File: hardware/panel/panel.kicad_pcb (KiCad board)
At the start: 2 copper layers, 62 x 104.3 mm, 1 part

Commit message: Panel: real MT1-MT4 standoff footprints (BOM/pos visible); combined file now flush V-cut seam
Standoff seats become SMD footprints with mask+paste aperture pads over the
back flood, so PCBWay's assembly sees 4 reflow nuts on the bottom side.
combine_boards.py butts the boards flush with one straight V-score at y=60 —
a sandable seam instead of mouse-bite nubs. Part number for the nut pends
sourcing (STANDOFF_PART/STANDOFF_LCSC in emit_board.py).
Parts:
- added MT1: SMTSO-M2.5-3ET, panel:SMT_Standoff_M2.5_D5.0mm, B.Cu at (5.64, 5.64)
- added MT2: SMTSO-M2.5-3ET, panel:SMT_Standoff_M2.5_D5.0mm, B.Cu at (56.4, 5.64)
- added MT3: SMTSO-M2.5-3ET, panel:SMT_Standoff_M2.5_D5.0mm, B.Cu at (5.64, 91.9)
- added MT4: SMTSO-M2.5-3ET, panel:SMT_Standoff_M2.5_D5.0mm, B.Cu at (53.4, 91.9)

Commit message: Panel: Wurth 9774030151R flat-bottom M2.5x3 standoffs — 6.0mm seats, ring paste, assembly data
Sourcing: no boss-free M2.5x3 exists except this Wurth WA-SMSI spacer
(Digi-Key, 48k stock). Seat grown 5.0->6.0mm per its land pattern; paste is
a 5.8/3.9mm ring so solder can't wick into the bottom-resident thread. Case
plan flag: screw tip must stop ~0.5mm short of the seat. MT1-4 now appear
in panel-bom/pos and the combined assembly BOM.
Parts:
- MT1: renamed from MT3; value SMTSO-M2.5-3ET -> 9774030151R; footprint panel:SMT_Standoff_M2.5_D5.0mm -> panel:SMT_Standoff_M2.5_D6.0mm
- MT2, MT4: value SMTSO-M2.5-3ET -> 9774030151R; footprint panel:SMT_Standoff_M2.5_D5.0mm -> panel:SMT_Standoff_M2.5_D6.0mm
- MT3: renamed from MT1; value SMTSO-M2.5-3ET -> 9774030151R; footprint panel:SMT_Standoff_M2.5_D5.0mm -> panel:SMT_Standoff_M2.5_D6.0mm
- moved MT1 86.3 mm to (5.64, 5.64)
- moved MT3 86.3 mm to (5.64, 91.9)

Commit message: Combined panel: flip art board face-down for one-sided assembly; nut 3D model
Panel mirrors left-right about its centreline inside the production panel,
so the standoff nuts reflow on the same face as the main board's SMT — a
single-side assembly order. Physical boards unchanged. Standoffs get a
5.1x3mm cylinder wrl so they show in 3D/renders.
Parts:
- moved MT2 86.3 mm to (56.4, 5.64)
- moved MT3 86.3 mm to (5.64, 91.9)
- moved MT1 50.7 mm to (5.64, 5.64)
- moved MT4 47.7 mm to (53.4, 91.9)
- renumbered MT2 to MT1, MT4 to MT2, MT1 to MT3, MT3 to MT4
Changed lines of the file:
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@@
+	(footprint "panel:SMT_Standoff_M2.5_D6.0mm"
+		(layer "B.Cu")
+		(at 5.6364 91.93)
+		(property "Reference" "MT3"
+			(at 0 0 0)
+			(layer "F.SilkS")
+			(hide yes)
+			(effects
+				(font
+					(size 1.27 1.27)
+				)
+			)
+		)
+		(property "Value" "9774030151R"
+			(at 0 0 0)
+			(layer "F.Fab")
+			(hide yes)
+			(effects
+				(font
+					(size 1.27 1.27)
+				)
+			)
+		)
+		(property "Datasheet" ""
+			(at 0 0 0)
+			(layer "F.Fab")
+			(hide yes)
+			(effects
+				(font
+					(size 1.27 1.27)
+				)
+			)
+		)
+		(property "Description" ""
+			(at 0 0 0)
+			(layer "F.Fab")
+			(hide yes)
+			(effects
+				(font
+					(size 1.27 1.27)
+				)
+			)
+		)
+		(attr smd)
+		(duplicate_pad_numbers_are_jumpers no)
+		(pad "" smd circle
+			(at 0 0)
+			(size 6 6)
+			(layers "B.Mask")
+		)
+		(embedded_fonts no)
+		(model "${KIPRJMOD}/standoff-m25x3.wrl"
+			(offset
+				(xyz 0 0 0)
+			)
+			(scale
+				(xyz 1 1 1)
+			)
+			(rotate
+				(xyz 0 0 0)
+			)
+		)
+	)
+	(footprint "panel:SMT_Standoff_M2.5_D6.0mm"
+		(layer "B.Cu")
+		(at 56.3636 5.6364)
+		(property "Reference" "MT2"
+			(at 0 0 0)
+			(layer "F.SilkS")
+			(hide yes)
+			(effects
+				(font
+					(size 1.27 1.27)
+				)
+			)
+		)
+		(property "Value" "9774030151R"
+			(at 0 0 0)
+			(layer "F.Fab")
+			(hide yes)
+			(effects
+				(font
+					(size 1.27 1.27)
+				)
+			)
+		)
+		(property "Datasheet" ""
+			(at 0 0 0)
+			(layer "F.Fab")
+			(hide yes)
+			(effects
+				(font
+					(size 1.27 1.27)
+				)
+			)
+		)
+		(property "Description" ""
+			(at 0 0 0)
+			(layer "F.Fab")
+			(hide yes)
+			(effects
+				(font
+					(size 1.27 1.27)
+				)
+			)
+		)
+		(attr smd)
+		(duplicate_pad_numbers_are_jumpers no)
+		(pad "" smd circle
+			(at 0 0)
+			(size 6 6)
+			(layers "B.Mask")
+		)
+		(embedded_fonts no)
+		(model "${KIPRJMOD}/standoff-m25x3.wrl"
+			(offset
+				(xyz 0 0 0)
+			)
+			(scale
+				(xyz 1 1 1)
+			)
+			(rotate
+				(xyz 0 0 0)
+			)
+		)
+	)
+	(footprint "panel:SMT_Standoff_M2.5_D6.0mm"
+		(layer "B.Cu")
+		(at 53.3636 91.93)
+		(property "Reference" "MT4"
+			(at 0 0 0)
+			(layer "F.SilkS")
+			(hide yes)
+			(effects
+				(font
+					(size 1.27 1.27)
+				)
+			)
+		)
+		(property "Value" "9774030151R"
+			(at 0 0 0)
+			(layer "F.Fab")
+			(hide yes)
+			(effects
+				(font
+					(size 1.27 1.27)
+				)
+			)
+		)
+		(property "Datasheet" ""
+			(at 0 0 0)
+			(layer "F.Fab")
+			(hide yes)
+			(effects
+				(font
+					(size 1.27 1.27)
+				)
+			)
+		)
+		(property "Description" ""
+			(at 0 0 0)
+			(layer "F.Fab")
+			(hide yes)
+			(effects
+				(font
+					(size 1.27 1.27)
+				)
+			)
+		)
+		(attr smd)
+		(duplicate_pad_numbers_are_jumpers no)
+		(pad "" smd circle
+			(at 0 0)
+			(size 6 6)
+			(layers "B.Mask")
+		)
+		(embedded_fonts no)
+		(model "${KIPRJMOD}/standoff-m25x3.wrl"
+			(offset
+				(xyz 0 0 0)
+			)
+			(scale
+				(xyz 1 1 1)
+			)
+			(rotate
+				(xyz 0 0 0)
+			)
+		)
+	)
 	(footprint "panel:SMT_Standoff_M2.5_D6.0mm"
 		(layer "B.Cu")
@@
 		)
 		(embedded_fonts no)
-	)
-	(footprint "panel:SMT_Standoff_M2.5_D6.0mm"
-		(layer "B.Cu")
-		(at 53.3636 91.93)
-		(property "Reference" "MT4"
-			(at 0 0 0)
-			(layer "F.SilkS")
-			(hide yes)
-			(effects
-				(font
-					(size 1.27 1.27)
-				)
-			)
-		)
-		(property "Value" "9774030151R"
-			(at 0 0 0)
-			(layer "F.Fab")
-			(hide yes)
-			(effects
-				(font
-					(size 1.27 1.27)
-				)
-			)
-		)
-		(property "Datasheet" ""
-			(at 0 0 0)
-			(layer "F.Fab")
-			(hide yes)
-			(effects
-				(font
-					(size 1.27 1.27)
-				)
-			)
-		)
-		(property "Description" ""
-			(at 0 0 0)
-			(layer "F.Fab")
-			(hide yes)
-			(effects
-				(font
-					(size 1.27 1.27)
-				)
-			)
-		)
-		(attr smd)
-		(duplicate_pad_numbers_are_jumpers no)
-		(pad "" smd circle
-			(at 0 0)
-			(size 6 6)
-			(layers "B.Mask")
-		)
-		(embedded_fonts no)
-	)
-	(footprint "panel:SMT_Standoff_M2.5_D6.0mm"
-		(layer "B.Cu")
-		(at 5.6364 91.93)
-		(property "Reference" "MT3"
-			(at 0 0 0)
-			(layer "F.SilkS")
-			(hide yes)
-			(effects
-				(font
-					(size 1.27 1.27)
-				)
-			)
-		)
-		(property "Value" "9774030151R"
-			(at 0 0 0)
-			(layer "F.Fab")
-			(hide yes)
-			(effects
-				(font
-					(size 1.27 1.27)
-				)
-			)
-		)
-		(property "Datasheet" ""
-			(at 0 0 0)
-			(layer "F.Fab")
-			(hide yes)
-			(effects
-				(font
-					(size 1.27 1.27)
-				)
-			)
-		)
-		(property "Description" ""
-			(at 0 0 0)
-			(layer "F.Fab")
-			(hide yes)
-			(effects
-				(font
-					(size 1.27 1.27)
-				)
-			)
-		)
-		(attr smd)
-		(duplicate_pad_numbers_are_jumpers no)
-		(pad "" smd circle
-			(at 0 0)
-			(size 6 6)
-			(layers "B.Mask")
-		)
-		(embedded_fonts no)
-	)
-	(footprint "panel:SMT_Standoff_M2.5_D6.0mm"
-		(layer "B.Cu")
-		(at 56.3636 5.6364)
-		(property "Reference" "MT2"
-			(at 0 0 0)
-			(layer "F.SilkS")
-			(hide yes)
-			(effects
-				(font
-					(size 1.27 1.27)
-				)
-			)
-		)
-		(property "Value" "9774030151R"
-			(at 0 0 0)
-			(layer "F.Fab")
-			(hide yes)
-			(effects
-				(font
-					(size 1.27 1.27)
-				)
-			)
-		)
-		(property "Datasheet" ""
-			(at 0 0 0)
-			(layer "F.Fab")
-			(hide yes)
-			(effects
-				(font
-					(size 1.27 1.27)
-				)
-			)
-		)
-		(property "Description" ""
-			(at 0 0 0)
-			(layer "F.Fab")
-			(hide yes)
-			(effects
-				(font
-					(size 1.27 1.27)
-				)
-			)
-		)
-		(attr smd)
-		(duplicate_pad_numbers_are_jumpers no)
-		(pad "" smd circle
-			(at 0 0)
-			(size 6 6)
-			(layers "B.Mask")
-		)
-		(embedded_fonts no)
+		(model "${KIPRJMOD}/standoff-m25x3.wrl"
+			(offset
+				(xyz 0 0 0)
+			)
+			(scale
+				(xyz 1 1 1)
+			)
+			(rotate
+				(xyz 0 0 0)
+			)
+		)
 	)
 	(gr_poly

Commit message: Standoffs: use KiCad's stock Wurth WA-SMSI H3mm STEP model (hand-written wrl never parsed)
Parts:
- moved MT3 47.7 mm to (5.64, 91.9)
- moved MT4 47.7 mm to (53.4, 91.9)
- renumbered MT4 to MT3, MT3 to MT4
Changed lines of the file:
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@@
+	(footprint "panel:SMT_Standoff_M2.5_D6.0mm"
+		(layer "B.Cu")
+		(at 53.3636 91.93)
+		(property "Reference" "MT4"
+			(at 0 0 0)
+			(layer "F.SilkS")
+			(hide yes)
+			(effects
+				(font
+					(size 1.27 1.27)
+				)
+			)
+		)
+		(property "Value" "9774030151R"
+			(at 0 0 0)
+			(layer "F.Fab")
+			(hide yes)
+			(effects
+				(font
+					(size 1.27 1.27)
+				)
+			)
+		)
+		(property "Datasheet" ""
+			(at 0 0 0)
+			(layer "F.Fab")
+			(hide yes)
+			(effects
+				(font
+					(size 1.27 1.27)
+				)
+			)
+		)
+		(property "Description" ""
+			(at 0 0 0)
+			(layer "F.Fab")
+			(hide yes)
+			(effects
+				(font
+					(size 1.27 1.27)
+				)
+			)
+		)
+		(attr smd)
+		(duplicate_pad_numbers_are_jumpers no)
+		(pad "" smd circle
+			(at 0 0)
+			(size 6 6)
+			(layers "B.Mask")
+		)
+		(embedded_fonts no)
+		(model "${KICAD10_3DMODEL_DIR}/Mounting_Wuerth.3dshapes/Mounting_Wuerth_WA-SMSI-M2.5_H3mm_9774030151.step"
+			(offset
+				(xyz 0 0 0)
+			)
+			(scale
+				(xyz 1 1 1)
+			)
+			(rotate
+				(xyz 0 0 0)
+			)
+		)
+	)
+	(footprint "panel:SMT_Standoff_M2.5_D6.0mm"
+		(layer "B.Cu")
+		(at 56.3636 5.6364)
+		(property "Reference" "MT2"
+			(at 0 0 0)
+			(layer "F.SilkS")
+			(hide yes)
+			(effects
+				(font
+					(size 1.27 1.27)
+				)
+			)
+		)
+		(property "Value" "9774030151R"
+			(at 0 0 0)
+			(layer "F.Fab")
+			(hide yes)
+			(effects
+				(font
+					(size 1.27 1.27)
+				)
+			)
+		)
+		(property "Datasheet" ""
+			(at 0 0 0)
+			(layer "F.Fab")
+			(hide yes)
+			(effects
+				(font
+					(size 1.27 1.27)
+				)
+			)
+		)
+		(property "Description" ""
+			(at 0 0 0)
+			(layer "F.Fab")
+			(hide yes)
+			(effects
+				(font
+					(size 1.27 1.27)
+				)
+			)
+		)
+		(attr smd)
+		(duplicate_pad_numbers_are_jumpers no)
+		(pad "" smd circle
+			(at 0 0)
+			(size 6 6)
+			(layers "B.Mask")
+		)
+		(embedded_fonts no)
+		(model "${KICAD10_3DMODEL_DIR}/Mounting_Wuerth.3dshapes/Mounting_Wuerth_WA-SMSI-M2.5_H3mm_9774030151.step"
+			(offset
+				(xyz 0 0 0)
+			)
+			(scale
+				(xyz 1 1 1)
+			)
+			(rotate
+				(xyz 0 0 0)
+			)
+		)
+	)
 	(footprint "panel:SMT_Standoff_M2.5_D6.0mm"
 		(layer "B.Cu")
@@
 		)
 		(embedded_fonts no)
-		(model "${KIPRJMOD}/standoff-m25x3.wrl"
+		(model "${KICAD10_3DMODEL_DIR}/Mounting_Wuerth.3dshapes/Mounting_Wuerth_WA-SMSI-M2.5_H3mm_9774030151.step"
 			(offset
 				(xyz 0 0 0)
@@
 	(footprint "panel:SMT_Standoff_M2.5_D6.0mm"
 		(layer "B.Cu")
-		(at 56.3636 5.6364)
-		(property "Reference" "MT2"
-			(at 0 0 0)
-			(layer "F.SilkS")
-			(hide yes)
-			(effects
-				(font
-					(size 1.27 1.27)
-				)
-			)
-		)
-		(property "Value" "9774030151R"
-			(at 0 0 0)
-			(layer "F.Fab")
-			(hide yes)
-			(effects
-				(font
-					(size 1.27 1.27)
-				)
-			)
-		)
-		(property "Datasheet" ""
-			(at 0 0 0)
-			(layer "F.Fab")
-			(hide yes)
-			(effects
-				(font
-					(size 1.27 1.27)
-				)
-			)
-		)
-		(property "Description" ""
-			(at 0 0 0)
-			(layer "F.Fab")
-			(hide yes)
-			(effects
-				(font
-					(size 1.27 1.27)
-				)
-			)
-		)
-		(attr smd)
-		(duplicate_pad_numbers_are_jumpers no)
-		(pad "" smd circle
-			(at 0 0)
-			(size 6 6)
-			(layers "B.Mask")
-		)
-		(embedded_fonts no)
-		(model "${KIPRJMOD}/standoff-m25x3.wrl"
-			(offset
-				(xyz 0 0 0)
-			)
-			(scale
-				(xyz 1 1 1)
-			)
-			(rotate
-				(xyz 0 0 0)
-			)
-		)
-	)
-	(footprint "panel:SMT_Standoff_M2.5_D6.0mm"
-		(layer "B.Cu")
-		(at 53.3636 91.93)
-		(property "Reference" "MT4"
-			(at 0 0 0)
-			(layer "F.SilkS")
-			(hide yes)
-			(effects
-				(font
-					(size 1.27 1.27)
-				)
-			)
-		)
-		(property "Value" "9774030151R"
-			(at 0 0 0)
-			(layer "F.Fab")
-			(hide yes)
-			(effects
-				(font
-					(size 1.27 1.27)
-				)
-			)
-		)
-		(property "Datasheet" ""
-			(at 0 0 0)
-			(layer "F.Fab")
-			(hide yes)
-			(effects
-				(font
-					(size 1.27 1.27)
-				)
-			)
-		)
-		(property "Description" ""
-			(at 0 0 0)
-			(layer "F.Fab")
-			(hide yes)
-			(effects
-				(font
-					(size 1.27 1.27)
-				)
-			)
-		)
-		(attr smd)
-		(duplicate_pad_numbers_are_jumpers no)
-		(pad "" smd circle
-			(at 0 0)
-			(size 6 6)
-			(layers "B.Mask")
-		)
-		(embedded_fonts no)
-		(model "${KIPRJMOD}/standoff-m25x3.wrl"
-			(offset
-				(xyz 0 0 0)
-			)
-			(scale
-				(xyz 1 1 1)
-			)
-			(rotate
-				(xyz 0 0 0)
-			)
-		)
-	)
-	(footprint "panel:SMT_Standoff_M2.5_D6.0mm"
-		(layer "B.Cu")
 		(at 5.6364 5.6364)
 		(property "Reference" "MT1"
@@
 		)
 		(embedded_fonts no)
-		(model "${KIPRJMOD}/standoff-m25x3.wrl"
-			(offset
-				(xyz 0 0 0)
+		(model "${KICAD10_3DMODEL_DIR}/Mounting_Wuerth.3dshapes/Mounting_Wuerth_WA-SMSI-M2.5_H3mm_9774030151.step"
+			(offset
+				(xyz 0 0 0)

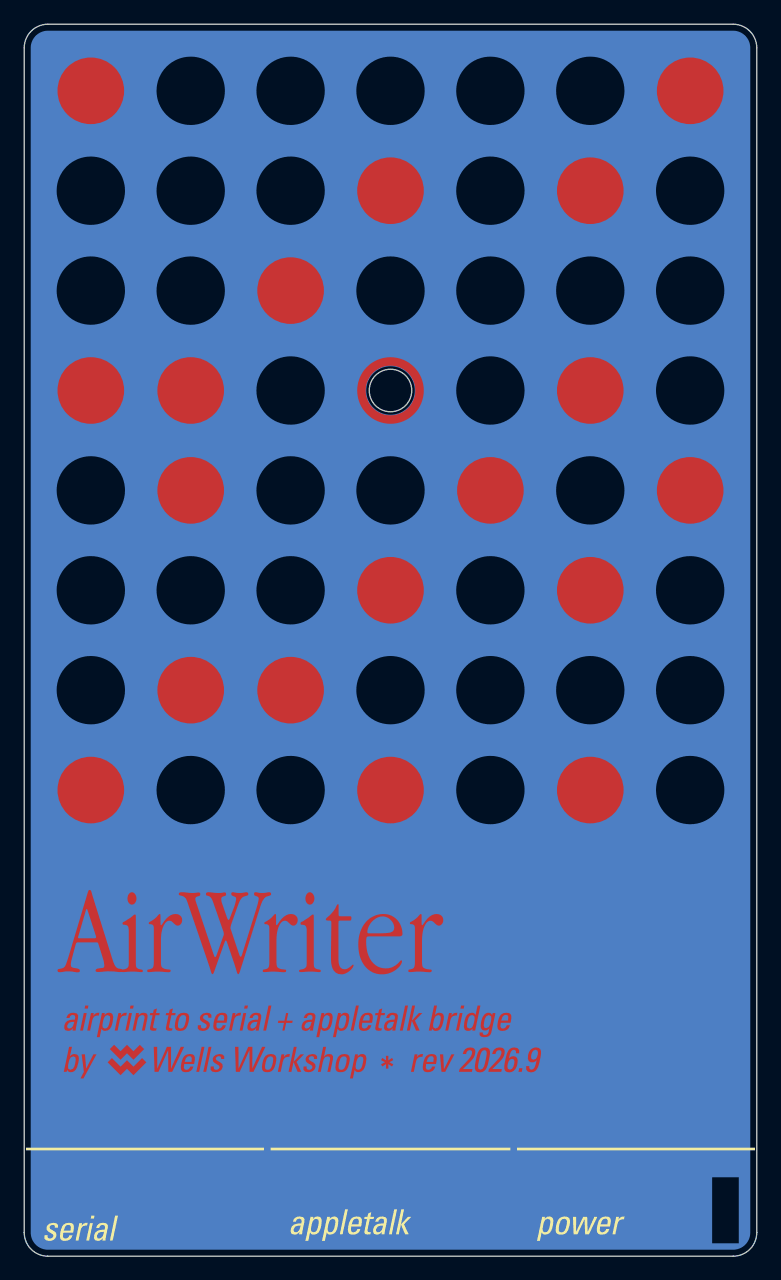
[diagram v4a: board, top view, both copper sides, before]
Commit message: Panel: test hole 3.6 -> 3.8mm for the TS-1002's 3.5+/-0.2mm shaft
Datasheet-verified: the switch is 16.0mm tall (correct for 0.5-1mm proud at
a 13.4-13.9mm lattice) but its shaft is 3.5mm — 3.6 left 0.05mm/side and a
tolerance-stack bind. Wells chose the bigger hole over a printed plunger.
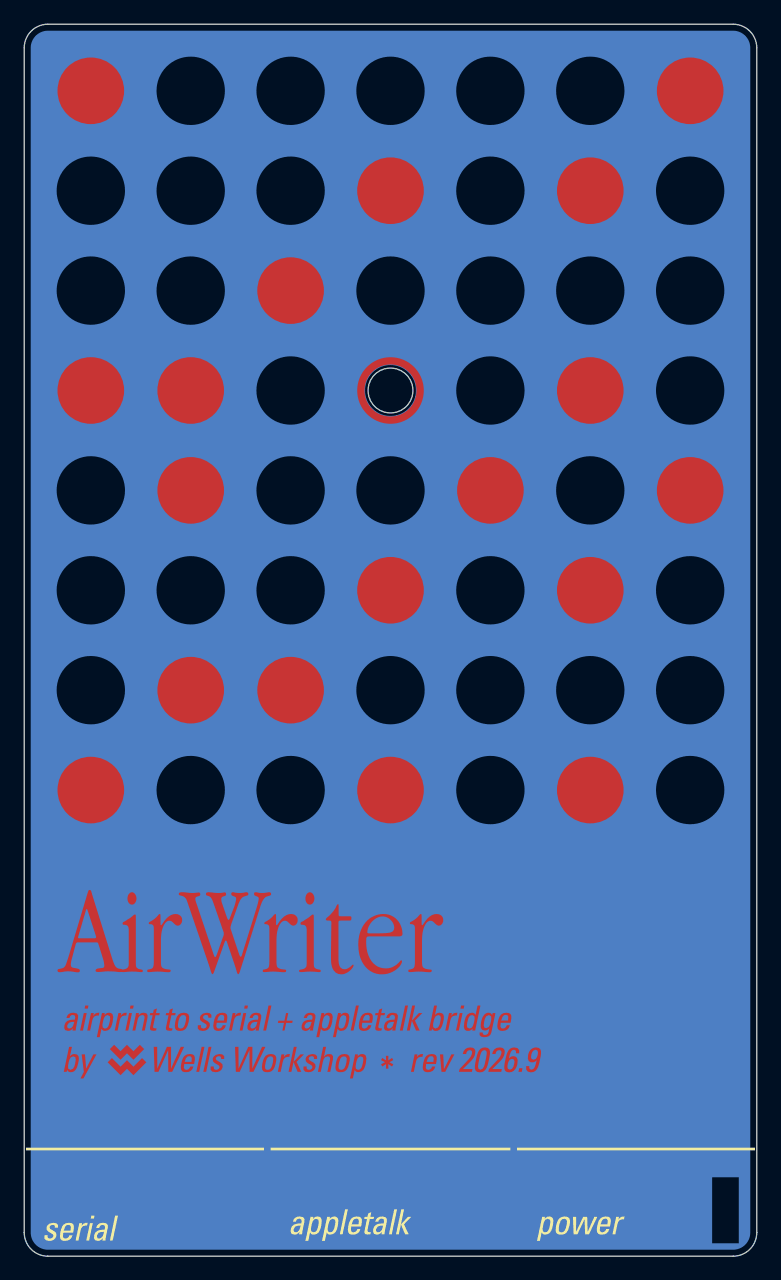
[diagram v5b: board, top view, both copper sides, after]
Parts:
- moved MT1 50.7 mm to (5.64, 5.64)
- moved MT2 50.7 mm to (56.4, 5.64)
- moved MT3 47.7 mm to (5.64, 91.9)
- moved MT4 47.7 mm to (53.4, 91.9)
- renumbered MT2 to MT1, MT1 to MT2, MT4 to MT3, MT3 to MT4

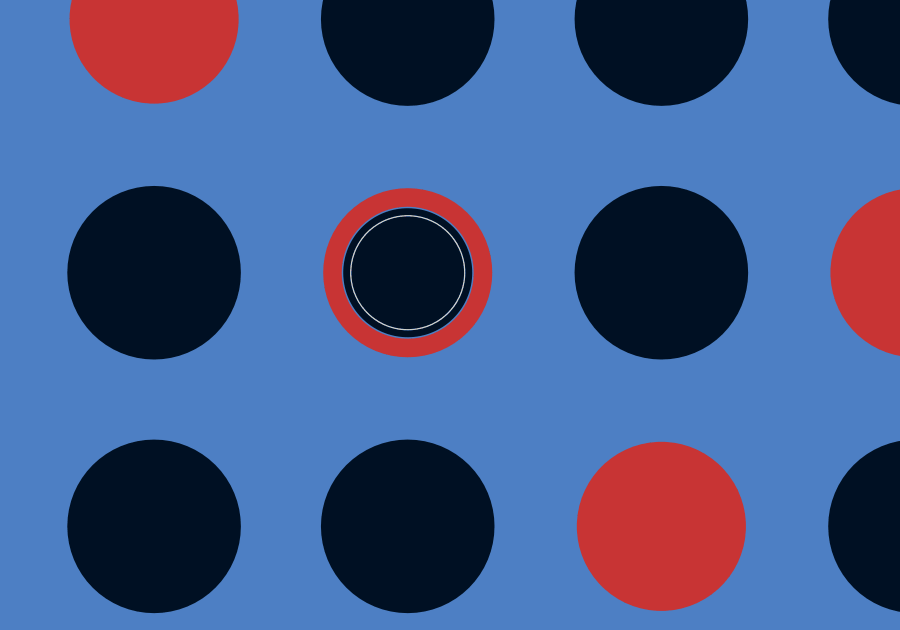
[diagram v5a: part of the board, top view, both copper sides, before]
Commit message: Panel: Frame 26 test dot — squared gold tab, glyphs clear of the 3.8mm hole
Wells redrew the test dot for the bigger hole: gold teardrop (disc + rounded
SE tab), hole marker at 3.83mm, 'test' knockout letters moved onto the tab.
Generator changes to carry it: knockout ownership reach 1.45r (glyphs live
past the disc edge now), glyph subtraction by boolean (edge-crossing holes
voided the whole opening), gold copper clipped around the NPTH, gold-art
mask opening keeps mask over knockout strokes.
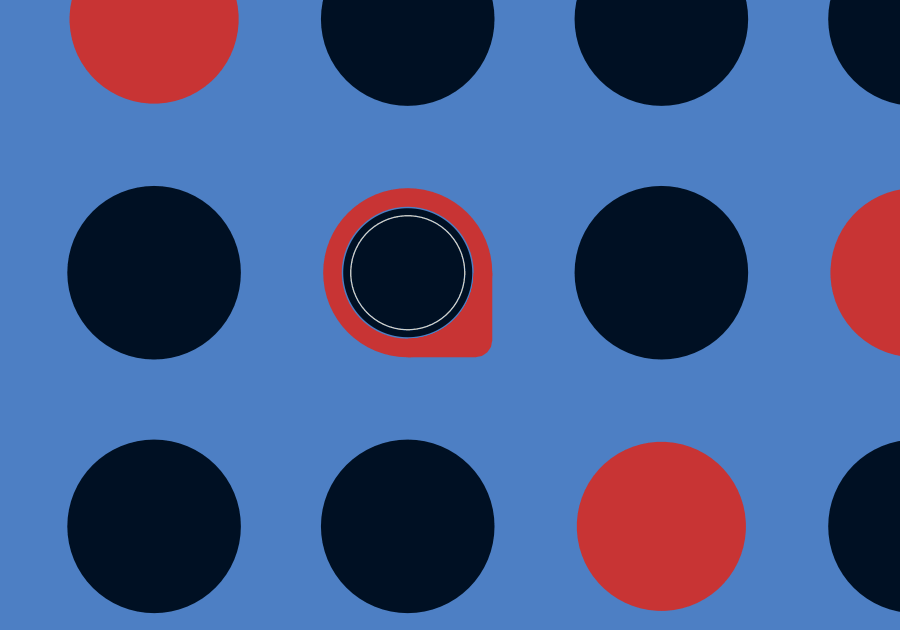
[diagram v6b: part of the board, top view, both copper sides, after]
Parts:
- moved MT1 98.6 mm to (5.64, 5.64)
- moved MT4 98.6 mm to (53.4, 91.9)
- renumbered MT4 to MT1, MT1 to MT4

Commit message: Panel: black ring around the test hole + repositioned glyphs (Frame 26 rev 2)
Mask now stays closed inside the black marker circle (3.83mm), so the
drill's surround reads black instead of a bare-FR4 cream ring; marker
diameter rides in panel_layout.json as hole_mark_dia. Wells's updated
export pulls the glyphs 3px left so the final t clears the tab edge.
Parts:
- moved MT1 98.6 mm to (5.64, 5.64)
- moved MT3 86.3 mm to (5.64, 91.9)
- moved MT4 47.7 mm to (53.4, 91.9)
- renumbered MT4 to MT1, MT1 to MT3, MT3 to MT4
